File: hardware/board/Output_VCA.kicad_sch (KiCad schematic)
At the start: 23 parts

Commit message: hardware: clear ERC issues, move BCM847 to the Winterbloom symbol library
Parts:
- Q?: symbol Carson's Schematic Symbols:BCM847 -> winterbloom:BCM847
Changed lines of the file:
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@@
     )
   )
-  (symbol (lib_name "BCM847_1") (lib_id "Carson's Schematic Symbols:BCM847") (at 147.32 104.14 270) (unit 1)
+  (symbol (lib_id "winterbloom:BCM847") (at 147.32 104.14 270) (unit 1)
     (in_bom yes) (on_board yes) (dnp no)
     (property "Reference" "Q?" (at 135.255 95.25 90)
@@
       (effects (font (size 1.27 1.27)) (justify left))
     )
-    (property "Footprint" "Package_TO_SOT_SMD:SOT-363_SC-70-6" (at 159.385 104.14 0)
+    (property "Footprint" "Package_TO_SOT_SMD:SOT-363_SC-70-6" (at 147.32 104.14 0)
       (effects (font (size 1.27 1.27)) hide)
     )
-    (property "Datasheet" "" (at 159.385 104.14 0)
+    (property "Datasheet" "https://assets.nexperia.com/documents/data-sheet/BCM847BS.pdf" (at 147.32 104.14 0)
       (effects (font (size 1.27 1.27)) hide)
     )

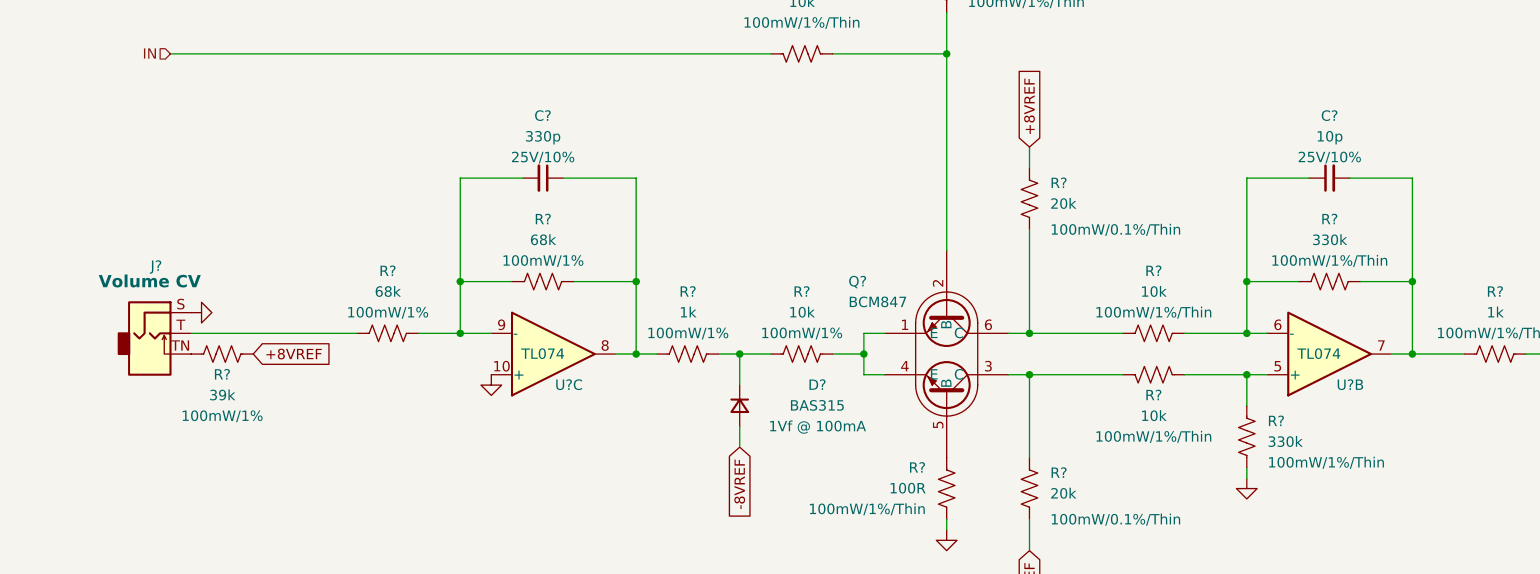
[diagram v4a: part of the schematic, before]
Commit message: hardware: add MPNs, DigiKey part numbers, and LCSC part numbers for all BOM items
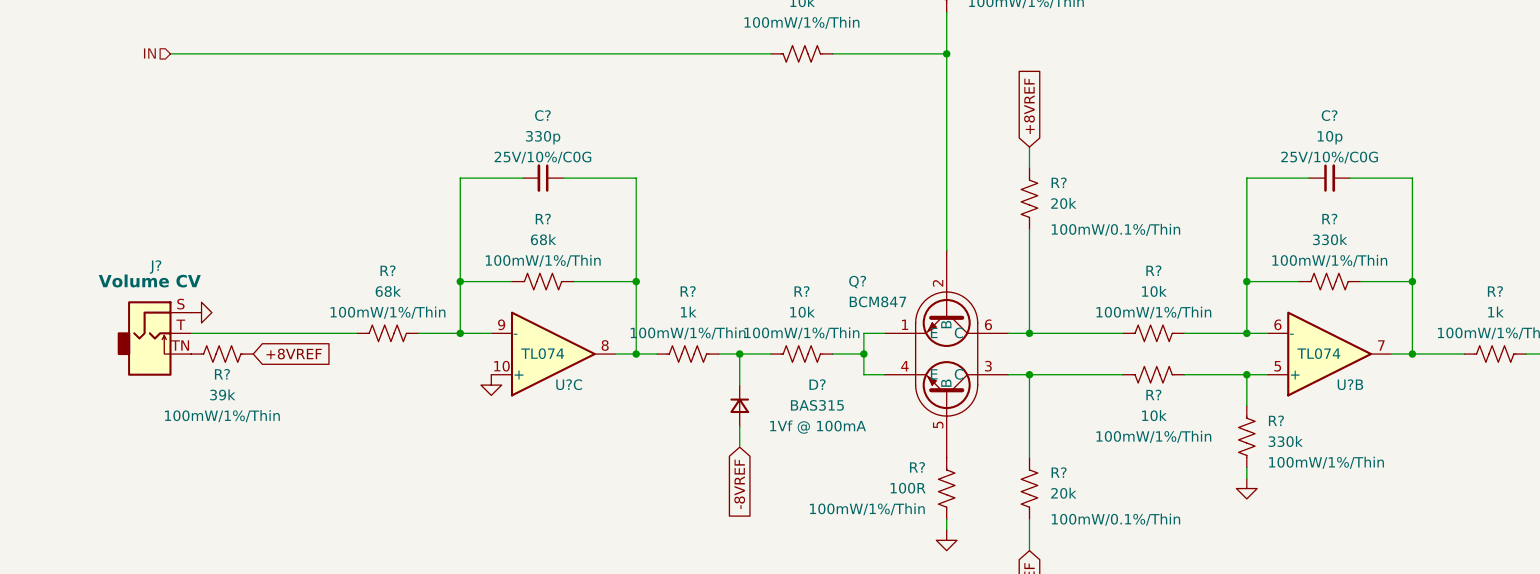
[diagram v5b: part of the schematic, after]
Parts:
- C?: DigiKey (none) -> 1276-1027-1-ND; LCSC (none) -> C1634; MPN (none) -> CL10C100JB8NNNC; Rating 25V/10% -> 25V/10%/C0G; Substitutes Allowed (none) -> Yes
- C?: DigiKey (none) -> 1276-1073-1-ND; LCSC (none) -> C1664; MPN (none) -> CL10C331JB8NNNC; Rating 25V/10% -> 25V/10%/C0G; Substitutes Allowed (none) -> Yes
- D?: DigiKey (none) -> 1727-4309-2-ND; LCSC (none) -> C109218; Substitutes Allowed (none) -> No
- Q?: Attention ! -> (none); DigiKey (none) -> 1727-5456-1-ND; LCSC (none) -> C396099; Substitutes Allowed (none) -> No
- R? (x2): DigiKey (none) -> YAG1582CT-ND; LCSC (none) -> C723637; MPN (none) -> RT0603BRD0720KL; Substitutes Allowed (none) -> Ask
- R? (x2): DigiKey (none) -> YAG5967CT-ND; LCSC (none) -> C706189; MPN (none) -> RT0603FRE0768KL; Rating 100mW/1% -> 100mW/1%/Thin; Substitutes Allowed (none) -> Yes
- R? (x3): DigiKey (none) -> YAG2321CT-ND; LCSC (none) -> C469659; MPN (none) -> RT0603FRE0710KL; Substitutes Allowed (none) -> Yes
- R? (x2): DigiKey (none) -> 13-RT0603FRE07330KLCT-ND; LCSC (none) -> C863745; MPN (none) -> RT0603FRE07330KL; Substitutes Allowed (none) -> Yes
- R? (x2): DigiKey (none) -> YAG1497CT-ND; LCSC (none) -> C122970; MPN (none) -> RT0603BRD07100RL; Substitutes Allowed (none) -> Ask
- R?: DigiKey (none) -> YAG2323TR-ND; LCSC (none) -> C375503; MPN (none) -> RT0603FRE071KL; Rating 100mW/1% -> 100mW/1%/Thin; Substitutes Allowed (none) -> Yes
- R?: DigiKey (none) -> YAG2321CT-ND; LCSC (none) -> C469659; MPN (none) -> RT0603FRE0710KL; Rating 100mW/1% -> 100mW/1%/Thin; Substitutes Allowed (none) -> Yes
- R?: DigiKey (none) -> YAG2323TR-ND; LCSC (none) -> C375503; MPN (none) -> RT0603FRE071KL; Substitutes Allowed (none) -> Yes
- R?: DigiKey (none) -> 13-RT0603FRE0739KLCT-ND; LCSC (none) -> C706166; MPN (none) -> RT0603FRE0739KL; Rating 100mW/1% -> 100mW/1%/Thin; Substitutes Allowed (none) -> Yes
- U? (x2): DigiKey (none) -> 296-7198-1-ND; LCSC (none) -> C96507; MPN TL074CPW -> TL074CPWR; Substitutes Allowed (none) -> No

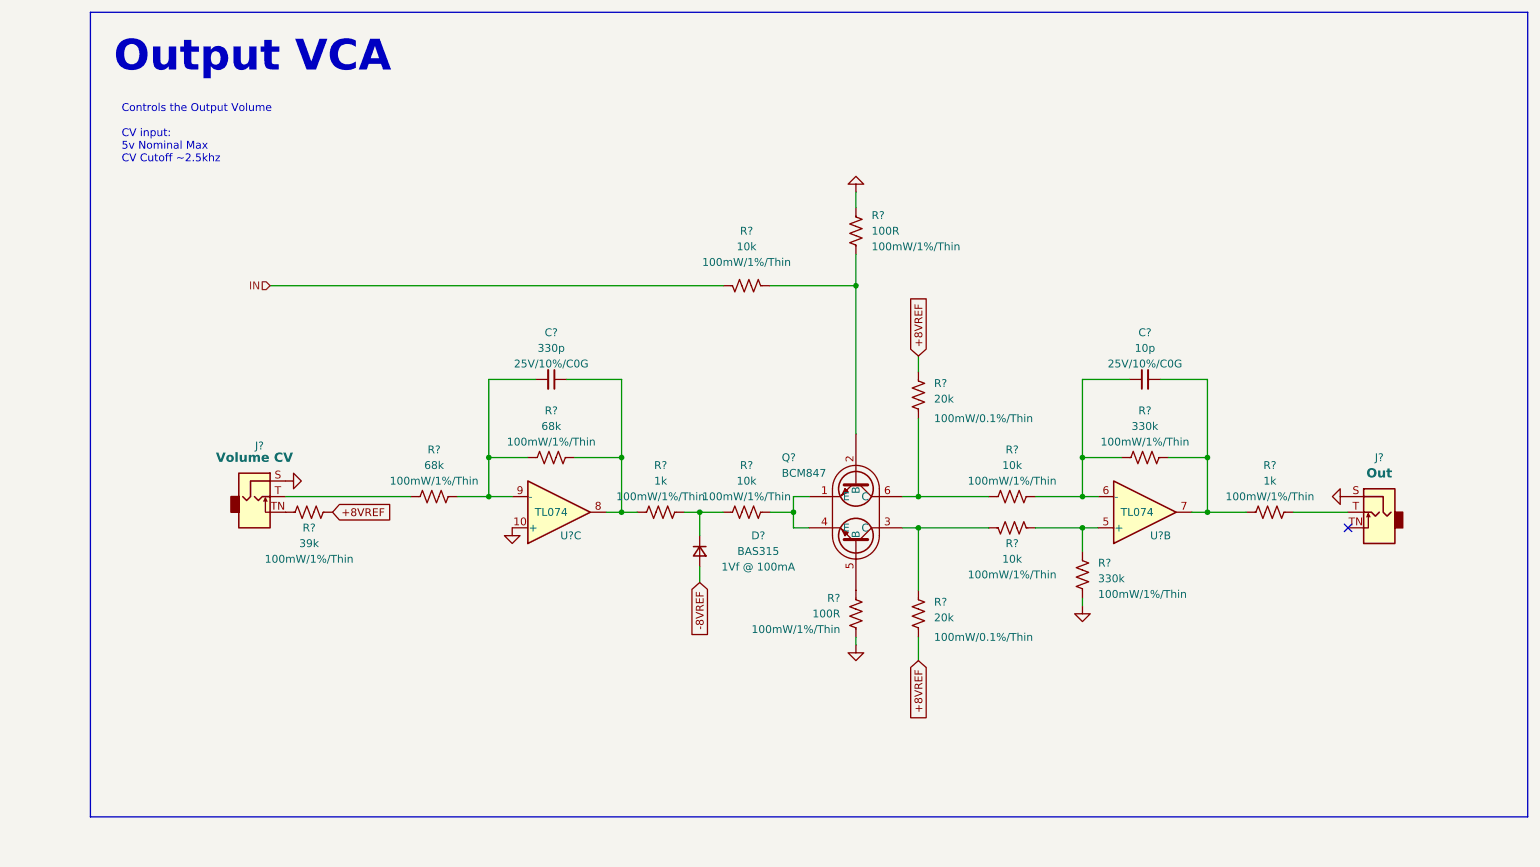
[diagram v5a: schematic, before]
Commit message: hardware: update schematic fonts/text sizes, some slight readability improvements
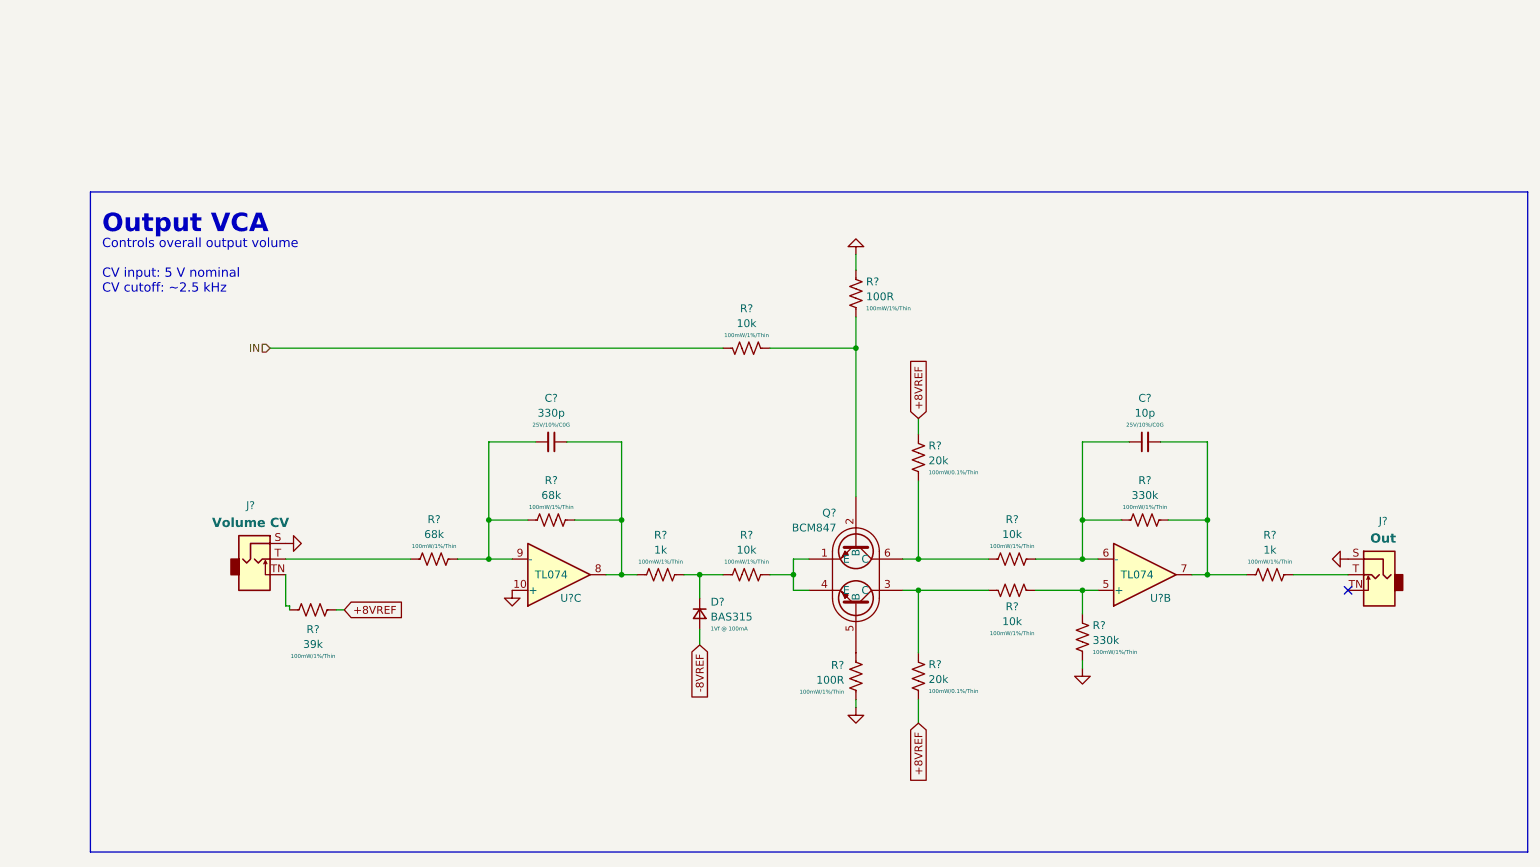
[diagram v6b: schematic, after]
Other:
- note added: "Controls overall output volume CV input: 5 V nominal CV cutoff: ~2.5 kHz"
- note removed: "Controls the Output Volume CV input: 5v Nominal Max CV Cutoff ~2.5khz"
- moved on the sheet: C?, D?, J?, Q?, R?, U?B, U?C

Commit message: hardware: use new Winterbloom sheet layout
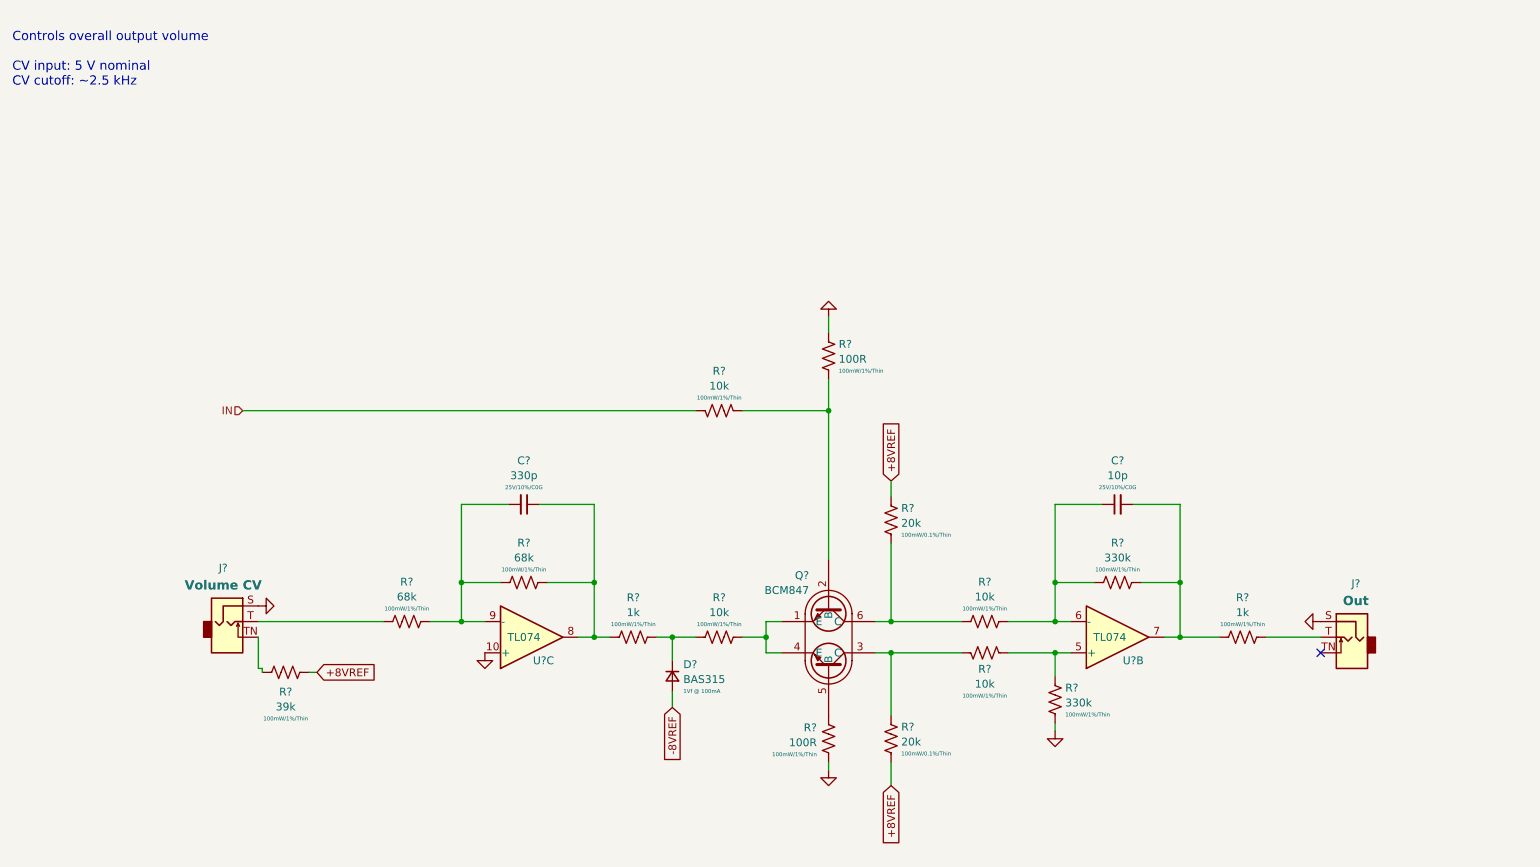
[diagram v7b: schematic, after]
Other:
- note removed: "Output VCA"
- moved on the sheet: C?, D?, J?, Q?, R?, U?B, U?C

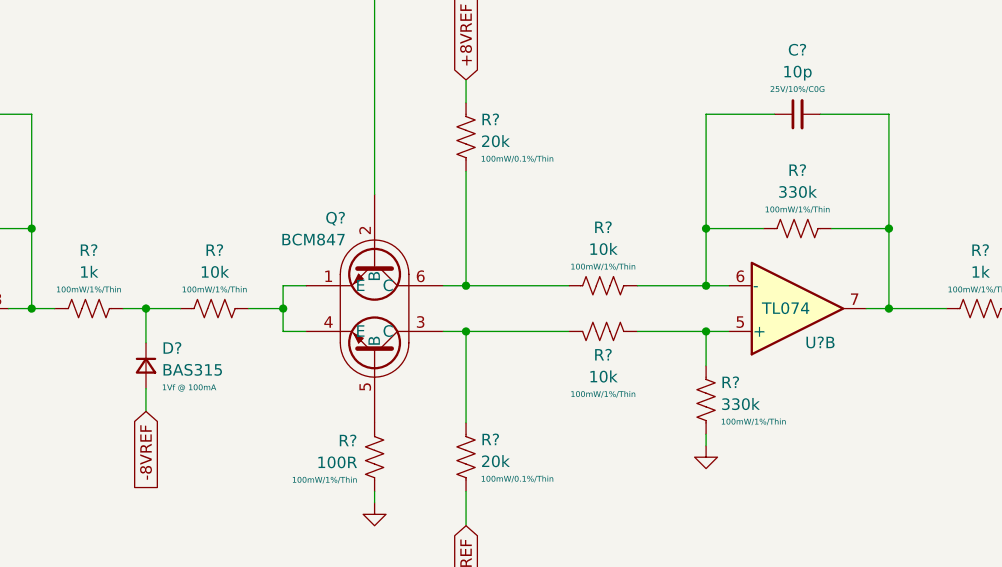
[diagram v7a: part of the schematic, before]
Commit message: hardware: finalize v3
- Updated version number and release date
- Swapped TL074C to TL074H
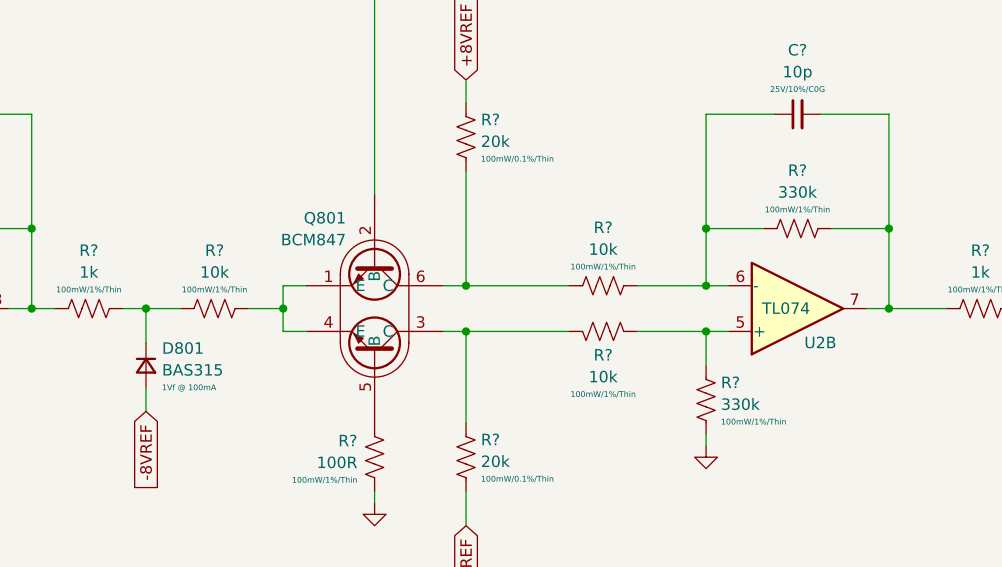
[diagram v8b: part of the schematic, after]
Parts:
- U2: renamed from U?; DigiKey 296-7198-1-ND -> 296-TL074HIPWRCT-ND; LCSC C96507 -> C4370424; MPN TL074CPWR -> TL074HIPWR; Notes (none) -> TL074H over TL074C due to better input offset voltage
- U?: DigiKey 296-7198-1-ND -> 296-TL074HIPWRCT-ND; LCSC C96507 -> C4370424; MPN TL074CPWR -> TL074HIPWR; Notes (none) -> TL074H over TL074C due to better input offset voltage
- gave numbers to parts that had none: 2
